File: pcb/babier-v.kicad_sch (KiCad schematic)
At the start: 69 parts, among them SW1 MX_SW_solder, SW10 MX_SW_solder, SW11 MX_SW_solder, SW12 MX_SW_solder, SW13 MX_SW_solder, SW14 MX_SW_solder, SW15 MX_SW_solder, SW16 MX_SW_solder, SW17 MX_SW_solder, SW18 MX_SW_solder, SW19 MX_SW_solder, SW2 MX_SW_solder, SW20 MX_SW_solder, SW21 MX_SW_solder, SW22 MX_SW_solder, SW23 MX_SW_solder, SW24 MX_SW_solder, SW25 MX_SW_solder, SW26 MX_SW_solder, SW27 MX_SW_solder, SW28 MX_SW_solder, SW29 MX_SW_solder, SW3 MX_SW_solder, SW30 MX_SW_solder, SW31 MX_SW_solder, SW32 MX_SW_solder, SW33 MX_SW_solder, SW34 MX_SW_solder, SW4 MX_SW_solder, SW5 MX_SW_solder, SW6 MX_SW_solder, SW7 MX_SW_solder, SW8 MX_SW_solder, SW9 MX_SW_solder, U1 Elite-C

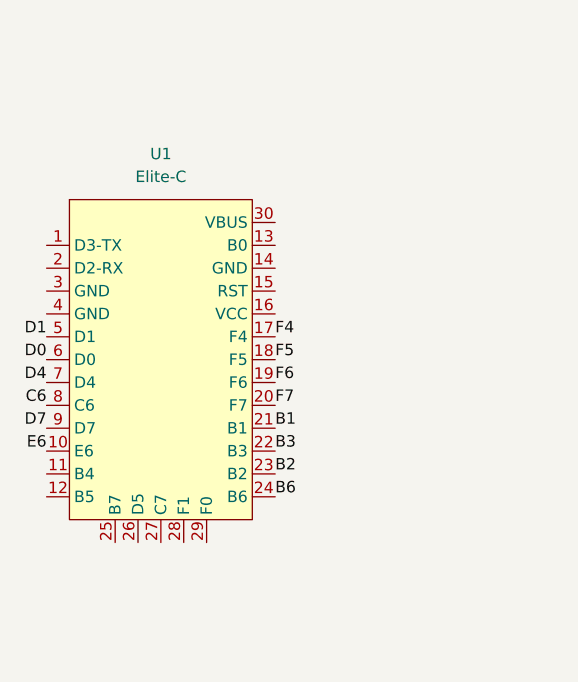
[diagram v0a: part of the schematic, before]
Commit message: small pcb changes, update todos
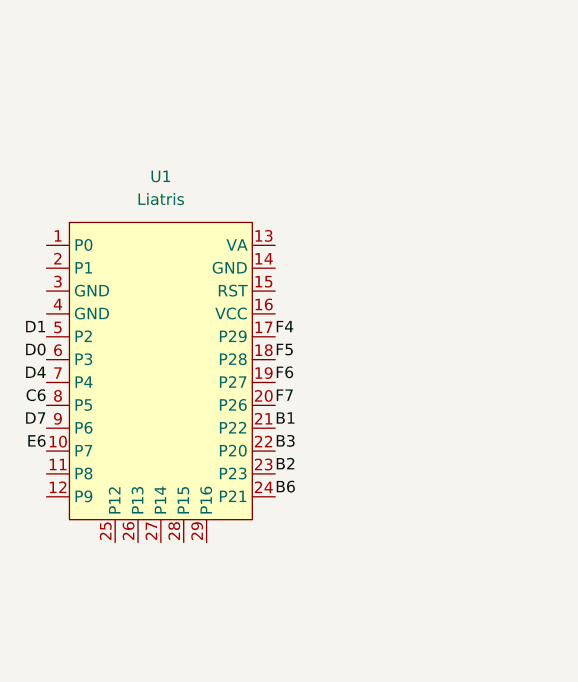
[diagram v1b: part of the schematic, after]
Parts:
- U1: value Elite-C -> Liatris; footprint PCM_marbastlib-xp-promicroish:Elite-C_ACH -> PCM_marbastlib-xp-promicroish:Liatris_AH_USBup; symbol PCM_marbastlib-promicroish:Elite-C -> PCM_marbastlib-promicroish:Liatris
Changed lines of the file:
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@@
 	(label "F6"
 		(at 62.23 58.42 0)
+		(fields_autoplaced yes)
 		(effects
 			(font
@@
 	(label "D7"
 		(at 36.83 63.5 180)
+		(fields_autoplaced yes)
 		(effects
 			(font
@@
 	(label "F5"
 		(at 62.23 55.88 0)
+		(fields_autoplaced yes)
 		(effects
 			(font
@@
 	(label "B2"
 		(at 62.23 68.58 0)
+		(fields_autoplaced yes)
 		(effects
 			(font
@@
 	(label "D4"
 		(at 36.83 58.42 180)
+		(fields_autoplaced yes)
 		(effects
 			(font
@@
 	(label "B3"
 		(at 62.23 66.04 0)
+		(fields_autoplaced yes)
 		(effects
 			(font
@@
 	(label "D0"
 		(at 36.83 55.88 180)
+		(fields_autoplaced yes)
 		(effects
 			(font
@@
 	(label "D1"
 		(at 36.83 53.34 180)
+		(fields_autoplaced yes)
 		(effects
 			(font
@@
 	(label "B6"
 		(at 62.23 71.12 0)
+		(fields_autoplaced yes)
 		(effects
 			(font
@@
 	(label "B1"
 		(at 62.23 63.5 0)
+		(fields_autoplaced yes)
 		(effects
 			(font
@@
 	(label "F7"
 		(at 62.23 60.96 0)
+		(fields_autoplaced yes)
 		(effects
 			(font
@@
 	(label "E6"
 		(at 36.83 66.04 180)
+		(fields_autoplaced yes)
 		(effects
 			(font
@@
 	(label "C6"
 		(at 36.83 60.96 180)
+		(fields_autoplaced yes)
 		(effects
 			(font
@@
 	(label "F4"
 		(at 62.23 53.34 0)
+		(fields_autoplaced yes)
 		(effects
 			(font
@@
 	)
 	(symbol
-		(lib_id "PCM_marbastlib-promicroish:Elite-C")
+		(lib_id "PCM_marbastlib-promicroish:Liatris")
 		(at 49.53 57.15 0)
 		(unit 1)
@@
 		(fields_autoplaced yes)
 		(property "Reference" "U1"
-			(at 49.53 33.02 0)
-			(effects
-				(font
-					(size 1.27 1.27)
-				)
-			)
-		)
-		(property "Value" "Elite-C"
 			(at 49.53 35.56 0)
 			(effects
@@
 			)
 		)
-		(property "Footprint" "PCM_marbastlib-xp-promicroish:Elite-C_ACH"
+		(property "Value" "Liatris"
+			(at 49.53 38.1 0)
+			(effects
+				(font
+					(size 1.27 1.27)
+				)
+			)
+		)
+		(property "Footprint" "PCM_marbastlib-xp-promicroish:Liatris_AH_USBup"
 			(at 49.53 87.63 0)
 			(effects
@@
 			)
 		)
-		(property "Description" "Symbol for an Elite-C"
+		(property "Description" "Symbol for a Splitkb Liatris"
 			(at 49.53 57.15 0)
 			(effects
@@
 		(pin "29"
 		)
-		(pin "30"
-		)
 		(pin "14"
